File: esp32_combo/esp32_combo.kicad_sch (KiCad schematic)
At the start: 34 parts, among them J1 TERM BLK 3.5MM 2P SIDE, J2 TERM BLK 3.5MM 6P SIDE, J3 TERM BLK 3.5MM 6P SIDE, J4 TERM BLK 3.5MM 3P SIDE, J5 TERM BLK 3.5MM 3P SIDE, J6 HDR SKT 5PIN VERT 2.54MM, J7 HDR SKT 7PIN VERT 2.54MM, J8 SKT 2x6PIN VERT 2.54MM, J9 HDR SKT 8PIN VERT 2.54MM, Q1 AS2302, SW1 SS12D10, U1 TB6612FNG Module, U2 ESP32 DEV KIT Module 30-pin, U3 LM2596 Module

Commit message: Logo
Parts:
- removed J7: HDR SKT 7PIN VERT 2.54MM, Connector_PinSocket_2.54mm:PinSocket_1x07_P2.54mm_Vertical, symbol Makerspet:Conn_01x07_Key2
- added J7: HDR SKT 6PIN VERT 2.54MM, Connector_PinSocket_2.54mm:PinSocket_1x06_P2.54mm_Vertical, symbol Connector_Generic:Conn_01x06
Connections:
- net +5V: now also J7.2 (Pin_2)
- net GND: now also J7.1 (Pin_1)
- net GPIO18: now also J7.4 (Pin_4)
- net GPIO27: now also J7.3 (Pin_3)
- net GPIO4: now also J7.6 (Pin_6)
- net GPIO5_BOOT_STRAP: now also J7.5 (Pin_5)
- net LDS_EN: now also J9.6 (Pin_6); no longer J9.8 (Pin_8)
- net LDS_PWM: now also J9.5 (Pin_5); no longer J9.6 (Pin_6)
- net LDS_RX: now also J9.8 (Pin_8); no longer J9.7 (Pin_7)
- net MOT: now reaches D1.2 (A), J9.4 (Pin_4), Q1.3 (D)
- net at R11.2: now also J9.7 (Pin_7); no longer J9.5 (Pin_5)
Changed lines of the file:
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@@
   (junction (at 194.31 78.74) (diameter 0) (color 0 0 0 0)
   )
+  (junction (at 242.57 120.65) (diameter 0) (color 0 0 0 0)
+  )
   (junction (at 149.86 153.67) (diameter 0) (color 0 0 0 0)
   )
@@
   )
   (junction (at 55.88 115.57) (diameter 0) (color 0 0 0 0)
-  )
-  (junction (at 243.84 29.21) (diameter 0) (color 0 0 0 0)
-  )
-  (junction (at 242.57 123.19) (diameter 0) (color 0 0 0 0)
   )
   (no_connect (at 34.29 24.13))
@@
     (stroke (width 0) (type default))
   )
-  (wire (pts (xy 243.84 26.67) (xy 243.84 29.21))
-    (stroke (width 0) (type default))
-  )
   (wire (pts (xy 86.36 115.57) (xy 86.36 116.84))
     (stroke (width 0) (type default))
@@
     (stroke (width 0) (type default))
   )
-  (wire (pts (xy 229.87 123.19) (xy 242.57 123.19))
+  (wire (pts (xy 229.87 123.19) (xy 250.19 123.19))
     (stroke (width 0) (type default))
   )
@@
     (stroke (width 0) (type default))
   )
-  (wire (pts (xy 242.57 123.19) (xy 242.57 151.13))
-    (stroke (width 0) (type default))
-  )
   (wire (pts (xy 86.36 105.41) (xy 86.36 97.79))
     (stroke (width 0) (type default))
@@
     (stroke (width 0) (type default))
   )
-  (wire (pts (xy 229.87 125.73) (xy 250.19 125.73))
-    (stroke (width 0) (type default))
-  )
   (wire (pts (xy 149.86 152.4) (xy 149.86 153.67))
     (stroke (width 0) (type default))
@@
     (stroke (width 0) (type default))
   )
+  (wire (pts (xy 229.87 120.65) (xy 242.57 120.65))
+    (stroke (width 0) (type default))
+  )
   (wire (pts (xy 189.23 35.56) (xy 189.23 44.45))
     (stroke (width 0) (type default))
@@
     (stroke (width 0) (type default))
   )
-  (wire (pts (xy 229.87 120.65) (xy 236.22 120.65))
-    (stroke (width 0) (type default))
-  )
   (wire (pts (xy 43.18 113.03) (xy 57.15 113.03))
     (stroke (width 0) (type default))
@@
     (stroke (width 0) (type default))
   )
-  (wire (pts (xy 245.11 26.67) (xy 243.84 26.67))
-    (stroke (width 0) (type default))
-  )
   (wire (pts (xy 34.29 57.15) (xy 30.48 57.15))
     (stroke (width 0) (type default))
@@
     (stroke (width 0) (type default))
   )
+  (wire (pts (xy 236.22 125.73) (xy 229.87 125.73))
+    (stroke (width 0) (type default))
+  )
   (wire (pts (xy 55.88 115.57) (xy 55.88 116.84))
     (stroke (width 0) (type default))
@@
     (stroke (width 0) (type default))
   )
-  (wire (pts (xy 236.22 120.65) (xy 236.22 118.11))
+  (wire (pts (xy 236.22 118.11) (xy 236.22 125.73))
     (stroke (width 0) (type default))
   )
@@
     (stroke (width 0) (type default))
   )
+  (wire (pts (xy 242.57 120.65) (xy 250.19 120.65))
+    (stroke (width 0) (type default))
+  )
   (wire (pts (xy 143.51 36.83) (xy 162.56 36.83))
     (stroke (width 0) (type default))
@@
     (stroke (width 0) (type default))
   )
+  (wire (pts (xy 242.57 120.65) (xy 242.57 151.13))
+    (stroke (width 0) (type default))
+  )
   (wire (pts (xy 13.97 54.61) (xy 34.29 54.61))
     (stroke (width 0) (type default))
@@
   )
   (wire (pts (xy 143.51 57.15) (xy 144.78 57.15))
-    (stroke (width 0) (type default))
-  )
-  (wire (pts (xy 242.57 123.19) (xy 250.19 123.19))
     (stroke (width 0) (type default))
   )
@@
     (effects (font (size 1.27 1.27)) (justify left bottom))
   )
+  (label "LDS_TX" (at 250.19 118.11 180) (fields_autoplaced)
+    (effects (font (size 1.27 1.27)) (justify right bottom))
+  )
   (label "ENC_A_LEFT" (at 13.97 31.75 0) (fields_autoplaced)
     (effects (font (size 1.27 1.27)) (justify left bottom))
@@
     (effects (font (size 1.27 1.27)) (justify right bottom))
   )
+  (label "MOT" (at 234.95 118.11 180) (fields_autoplaced)
+    (effects (font (size 1.27 1.27)) (justify right bottom))
+  )
   (label "CW_LEFT" (at 162.56 24.13 180) (fields_autoplaced)
     (effects (font (size 1.27 1.27)) (justify right bottom))
   )
-  (label "LDS_TX" (at 250.19 118.11 180) (fields_autoplaced)
-    (effects (font (size 1.27 1.27)) (justify right bottom))
-  )
   (label "M+LEFT" (at 49.53 132.08 0) (fields_autoplaced)
     (effects (font (size 1.27 1.27)) (justify left bottom))
@@
     (effects (font (size 1.27 1.27)) (justify right bottom))
   )
+  (label "LDS_RX" (at 250.19 128.27 180) (fields_autoplaced)
+    (effects (font (size 1.27 1.27)) (justify right bottom))
+  )
   (label "ENC_B_RIGHT" (at 125.73 139.7 180) (fields_autoplaced)
     (effects (font (size 1.27 1.27)) (justify right bottom))
@@
     (effects (font (size 1.27 1.27)) (justify left bottom))
   )
-  (label "LDS_PWM" (at 250.19 123.19 180) (fields_autoplaced)
-    (effects (font (size 1.27 1.27)) (justify right bottom))
-  )
   (label "CW_LEFT" (at 109.22 110.49 180) (fields_autoplaced)
     (effects (font (size 1.27 1.27)) (justify right bottom))
@@
     (effects (font (size 1.27 1.27)) (justify left bottom))
   )
-  (label "LDS_RX" (at 250.19 125.73 180) (fields_autoplaced)
-    (effects (font (size 1.27 1.27)) (justify right bottom))
-  )
   (label "I2C_SDA" (at 179.07 78.74 0) (fields_autoplaced)
     (effects (font (size 1.27 1.27)) (justify left bottom))
@@
     (effects (font (size 1.27 1.27)) (justify left bottom))
   )
+  (label "LDS_PWM" (at 250.19 120.65 180) (fields_autoplaced)
+    (effects (font (size 1.27 1.27)) (justify right bottom))
+  )
   (label "I2C_INT" (at 179.07 81.28 0) (fields_autoplaced)
     (effects (font (size 1.27 1.27)) (justify left bottom))
@@
     (effects (font (size 1.27 1.27)) (justify right bottom))
   )
+  (label "LDS_EN" (at 250.19 123.19 180) (fields_autoplaced)
+    (effects (font (size 1.27 1.27)) (justify right bottom))
+  )
   (label "PWM_LEFT" (at 109.22 107.95 180) (fields_autoplaced)
     (effects (font (size 1.27 1.27)) (justify right bottom))
@@
   )
   (label "GPIO4" (at 162.56 49.53 180) (fields_autoplaced)
-    (effects (font (size 1.27 1.27)) (justify right bottom))
-  )
-  (label "LDS_EN" (at 250.19 128.27 180) (fields_autoplaced)
     (effects (font (size 1.27 1.27)) (justify right bottom))
   )
@@
         (path "/e24ae185-8f18-408c-aee8-f727519bade3"
           (reference "#PWR08") (unit 1)
-        )
-      )
-    )
-  )
-  (symbol (lib_id "Makerspet:Conn_01x07_Key2") (at 250.19 34.29 0) (unit 1)
-    (in_bom yes) (on_board yes) (dnp no)
-    (property "Reference" "J7" (at 249.174 23.622 0)
-      (effects (font (size 1.27 1.27)) (justify left))
-    )
-    (property "Value" "HDR SKT 7PIN VERT 2.54MM" (at 254 47.498 90)
-      (effects (font (size 1.27 1.27)) (justify left))
-    )
-    (property "Footprint" "Connector_PinSocket_2.54mm:PinSocket_1x07_P2.54mm_Vertical" (at 250.19 34.29 0)
-      (effects (font (size 1.27 1.27)) hide)
-    )
-    (property "Datasheet" "~" (at 250.19 34.29 0)
-      (effects (font (size 1.27 1.27)) hide)
-    )
-    (pin "5")
-    (pin "3")
-    (pin "2")
-    (pin "6")
-    (pin "1")
-    (pin "4")
-    (pin "7")
-    (instances
-      (project "esp32_combo"
-        (path "/e24ae185-8f18-408c-aee8-f727519bade3"
-          (reference "J7") (unit 1)
         )
       )
@@
         )
       )
+    )
+  )
+  (symbol (lib_id "Connector_Generic:Conn_01x06") (at 250.19 34.29 0) (unit 1)
+    (in_bom yes) (on_board yes) (dnp no)
+    (property "Reference" "J7" (at 248.92 25.4 0)
+      (effects (font (size 1.27 1.27)) (justify left))
+    )
+    (property "Value" "HDR SKT 6PIN VERT 2.54MM" (at 254 46.99 90)
+      (effects (font (size 1.27 1.27)) (justify left))
+    )
+    (property "Footprint" "Connector_PinSocket_2.54mm:PinSocket_1x06_P2.54mm_Vertical" (at 250.19 34.29 0)
+      (effects (font (size 1.27 1.27)) hide)
+    )
+    (property "Datasheet" "~" (at 250.19 34.29 0)
+      (effects (font (size 1.27 1.27)) hide)
+    )
+    (pin "6")
+    (pin "3")
+    (pin "4")
+    (pin "1")
+    (pin "5")
+    (pin "2")
+    (instances
+      (project "esp32_combo"
+        (path "/e24ae185-8f18-408c-aee8-f727519bade3"
+          (reference "J7") (unit 1)
+        )
+      )

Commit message: Combo tweaks
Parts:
- removed C2: 100uF 16V, Capacitor_Tantalum_SMD:CP_EIA-7343-15_Kemet-W, symbol Device:C_Polarized_Small_US
- C1: value 22uF -> 22uF 6.3V
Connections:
- net EA_LEFT renamed EA_LEFT_FG
- net EA_RIGHT renamed EA_RIGHT_FG
- net ENC_A_LEFT renamed ENC_A_LEFT_FG
- net ENC_A_RIGHT renamed ENC_A_RIGHT_FG
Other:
- note added: "INPUT VOLTAGE 9..13.5V WHEN USING TB6612FNG - Use 12V brushed motors Max input current approx. 3.0A with both motors stalled Safety - motor power overcurrent protection using a fuse Use a slow-blow fuse to prevent inrush current tripping the fuse - battery input reverse polarity protection using a Schottki diode - TODO input overvoltage LM2596 40V max; motors not protected - TODO 5V output LM2596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"
- note removed: "Input voltage 9..13.5V - Use 12V motors Max input current approx. 3.0A with both motors stalled Safety - motor power overcurrent protection using a fuse Use a slow-blow fuse to prevent inrush current tripping the fuse - battery input reverse polarity protection using a Schottki diode - TODO input overvoltage LM2596 40V max; motors not protected - TODO 5V output LM2596 provides current limit, shor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"
- moved on the sheet: C1

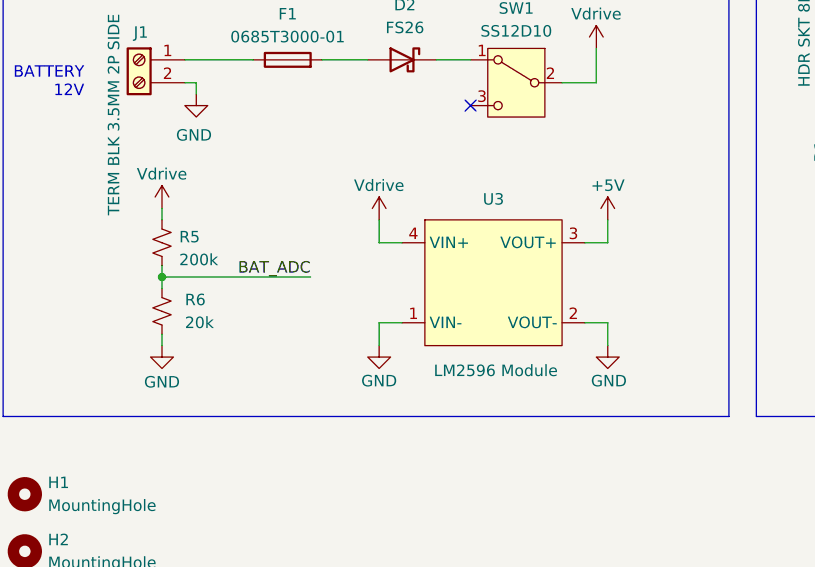
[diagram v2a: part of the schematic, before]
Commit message: 1% resistor divider
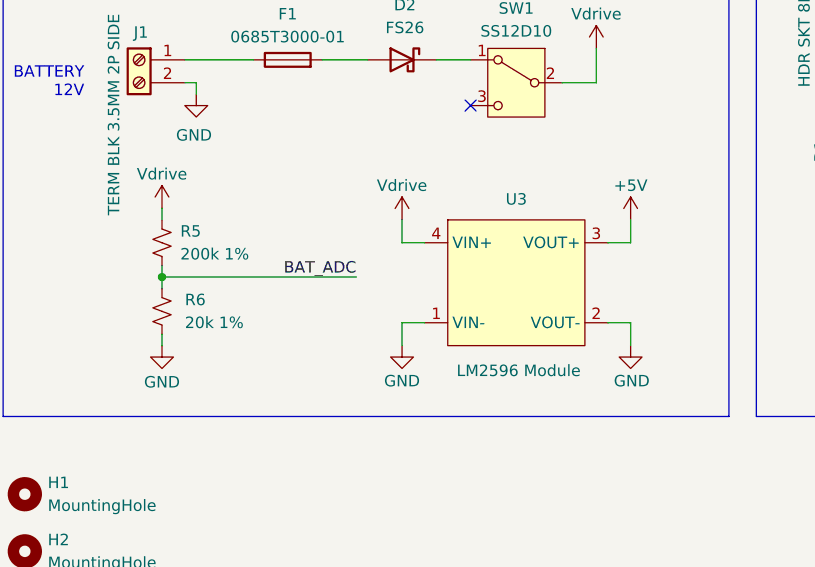
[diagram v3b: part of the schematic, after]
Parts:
- R5: value 200k -> 200k 1%
- R6: value 20k -> 20k 1%
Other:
- moved on the sheet: U3
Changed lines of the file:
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@@
 	(wire
 		(pts
-			(xy 173.99 149.86) (xy 176.53 149.86)
+			(xy 176.53 149.86) (xy 179.07 149.86)
 		)
 		(stroke
@@
 	(wire
 		(pts
-			(xy 173.99 158.75) (xy 176.53 158.75)
+			(xy 176.53 158.75) (xy 179.07 158.75)
 		)
 		(stroke
@@
 	(wire
 		(pts
-			(xy 173.99 161.29) (xy 173.99 158.75)
+			(xy 176.53 161.29) (xy 176.53 158.75)
 		)
 		(stroke
@@
 	(wire
 		(pts
-			(xy 199.39 161.29) (xy 199.39 158.75)
+			(xy 201.93 161.29) (xy 201.93 158.75)
 		)
 		(stroke
@@
 	(wire
 		(pts
-			(xy 196.85 149.86) (xy 199.39 149.86)
+			(xy 199.39 149.86) (xy 201.93 149.86)
 		)
 		(stroke
@@
 	(wire
 		(pts
-			(xy 196.85 158.75) (xy 199.39 158.75)
+			(xy 199.39 158.75) (xy 201.93 158.75)
 		)
 		(stroke
@@
 	(wire
 		(pts
-			(xy 173.99 147.32) (xy 173.99 149.86)
+			(xy 176.53 147.32) (xy 176.53 149.86)
 		)
 		(stroke
@@
 	(wire
 		(pts
-			(xy 149.86 153.67) (xy 166.37 153.67)
+			(xy 149.86 153.67) (xy 171.45 153.67)
 		)
 		(stroke
@@
 	(wire
 		(pts
-			(xy 199.39 147.32) (xy 199.39 149.86)
+			(xy 201.93 147.32) (xy 201.93 149.86)
 		)
 		(stroke
@@
 		)
 	)
+	(label "BAT_ADC"
+		(at 171.45 153.67 180)
+		(fields_autoplaced yes)
+		(effects
+			(font
+				(size 1.27 1.27)
+			)
+			(justify right bottom)
+		)
+	)
 	(label "M+LEFT"
 		(at 43.18 110.49 0)
@@
 		)
 	)
-	(label "BAT_ADC"
-		(at 166.37 153.67 180)
-		(fields_autoplaced yes)
-		(effects
-			(font
-				(size 1.27 1.27)
-			)
-			(justify right bottom)
-		)
-	)
 	(label "LDS_RX"
 		(at 250.19 128.27 180)
@@
 	(symbol
 		(lib_id "power:GND")
-		(at 173.99 161.29 0)
+		(at 176.53 161.29 0)
 		(unit 1)
 		(exclude_from_sim no)
@@
 		(dnp no)
 		(property "Reference" "#PWR022"
-			(at 173.99 167.64 0)
+			(at 176.53 167.64 0)
 			(effects
 				(font
@@
 		)
 		(property "Value" "GND"
-			(at 173.99 165.227 0)
+			(at 176.53 165.227 0)
 			(effects
 				(font
@@
 		)
 		(property "Footprint" ""
-			(at 173.99 161.29 0)
+			(at 176.53 161.29 0)
 			(effects
 				(font
@@
 		)
 		(property "Datasheet" ""
-			(at 173.99 161.29 0)
+			(at 176.53 161.29 0)
 			(effects
 				(font
@@
 		)
 		(property "Description" "Power symbol creates a global label with name \"GND\" , ground"
-			(at 173.99 161.29 0)
+			(at 176.53 161.29 0)
 			(effects
 				(font
@@
 	(symbol
 		(lib_id "Makerspet:LM2596 Module")
-		(at 186.69 144.78 0)
+		(at 189.23 144.78 0)
 		(unit 1)
 		(exclude_from_sim no)
@@
 		(dnp no)
 		(property "Reference" "U3"
-			(at 186.69 145.034 0)
+			(at 189.23 145.034 0)
 			(effects
 				(font
@@
 		)
 		(property "Value" "LM2596 Module"
-			(at 186.944 164.084 0)
+			(at 189.484 164.084 0)
 			(effects
 				(font
@@
 		)
 		(property "Footprint" "Makerspet:LM2596 Module SMD"
-			(at 186.69 143.51 0)
+			(at 189.23 143.51 0)
 			(effects
 				(font
@@
 		)
 		(property "Datasheet" ""
-			(at 186.69 144.78 0)
+			(at 189.23 144.78 0)
 			(effects
 				(font
@@
 		)
 		(property "Description" ""
-			(at 186.69 144.78 0)
+			(at 189.23 144.78 0)
 			(effects
 				(font
@@
 		)
 		(property "Type" ""
-			(at 186.69 142.24 0)
+			(at 189.23 142.24 0)
 			(effects
 				(font
@@
 		)
 		(property "Link" "https://www.amazon.com/Zixtec-LM2596-Converter-Module-1-25V-30V/dp/B07VVXF7YX/"
-			(at 187.96 140.335 0)
+			(at 190.5 140.335 0)
 			(effects
 				(font
@@
 		(fields_autoplaced yes)
 		(property "Reference" "R6"
-			(at 152.4 156.21 0)
+			(at 152.4 156.2099 0)
 			(effects
 				(font
@@
 			)
 		)
-		(property "Value" "20k"
-			(at 152.4 158.75 0)
+		(property "Value" "20k 1%"
+			(at 152.4 158.7499 0)
 			(effects
 				(font
@@
 	(symbol
 		(lib_id "power:Vdrive")
-		(at 173.99 147.32 0)
+		(at 176.53 147.32 0)
 		(unit 1)
 		(exclude_from_sim no)
@@
 		(dnp no)
 		(property "Reference" "#PWR021"
-			(at 168.91 151.13 0)
+			(at 171.45 151.13 0)
 			(effects
 				(font
@@
 		)
 		(property "Value" "Vdrive"
-			(at 173.99 143.51 0)
+			(at 176.53 143.51 0)
 			(effects
 				(font
@@
 		)
 		(property "Footprint" ""
-			(at 173.99 147.32 0)
+			(at 176.53 147.32 0)
 			(effects
 				(font
@@
 		)
 		(property "Datasheet" ""
-			(at 173.99 147.32 0)
+			(at 176.53 147.32 0)
 			(effects
 				(font
@@
 		)
 		(property "Description" "Power symbol creates a global label with name \"Vdrive\""
-			(at 173.99 147.32 0)
+			(at 176.53 147.32 0)
 			(effects
 				(font
@@
 		(on_board yes)
 		(dnp no)
-		(fields_autoplaced yes)
 		(property "Reference" "R5"
-			(at 151.765 149.225 0)
+			(at 151.892 148.59 0)
 			(effects
 				(font
@@
 			)
 		)
-		(property "Value" "200k"
-			(at 151.765 151.765 0)
+		(property "Value" "200k 1%"
+			(at 151.892 151.13 0)
 			(effects
 				(font
@@
 	(symbol
 		(lib_id "power:GND")
-		(at 199.39 161.29 0)
+		(at 201.93 161.29 0)
 		(unit 1)
 		(exclude_from_sim no)
@@
 		(dnp no)
 		(property "Reference" "#PWR028"
-			(at 199.39 167.64 0)
+			(at 201.93 167.64 0)
 			(effects
 				(font
@@
 		)
 		(property "Value" "GND"
-			(at 199.517 165.227 0)
+			(at 202.057 165.227 0)
 			(effects
 				(font
@@
 		)
 		(property "Footprint" ""
-			(at 199.39 161.29 0)
+			(at 201.93 161.29 0)
 			(effects
 				(font
@@
 		)
 		(property "Datasheet" ""
-			(at 199.39 161.29 0)
+			(at 201.93 161.29 0)
 			(effects
 				(font
@@
 		)
 		(property "Description" "Power symbol creates a global label with name \"GND\" , ground"
-			(at 199.39 161.29 0)
+			(at 201.93 161.29 0)
 			(effects
 				(font
@@
 	(symbol
 		(lib_id "power:+5V")
-		(at 199.39 147.32 0)
+		(at 201.93 147.32 0)
 		(unit 1)
 		(exclude_from_sim no)
@@
 		(fields_autoplaced yes)
 		(property "Reference" "#PWR027"
-			(at 199.39 151.13 0)
+			(at 201.93 151.13 0)
 			(effects
 				(font
@@
 		)
 		(property "Value" "+5V"
-			(at 199.39 143.51 0)
+			(at 201.93 143.51 0)
 			(effects
 				(font
@@
 		)
 		(property "Footprint" ""
-			(at 199.39 147.32 0)
+			(at 201.93 147.32 0)
 			(effects
 				(font
@@
 		)
 		(property "Datasheet" ""
-			(at 199.39 147.32 0)
+			(at 201.93 147.32 0)
 			(effects
 				(font
@@
 		)
 		(property "Description" "Power symbol creates a global label with name \"+5V\""
-			(at 199.39 147.32 0)
+			(at 201.93 147.32 0)
 			(effects
 				(font

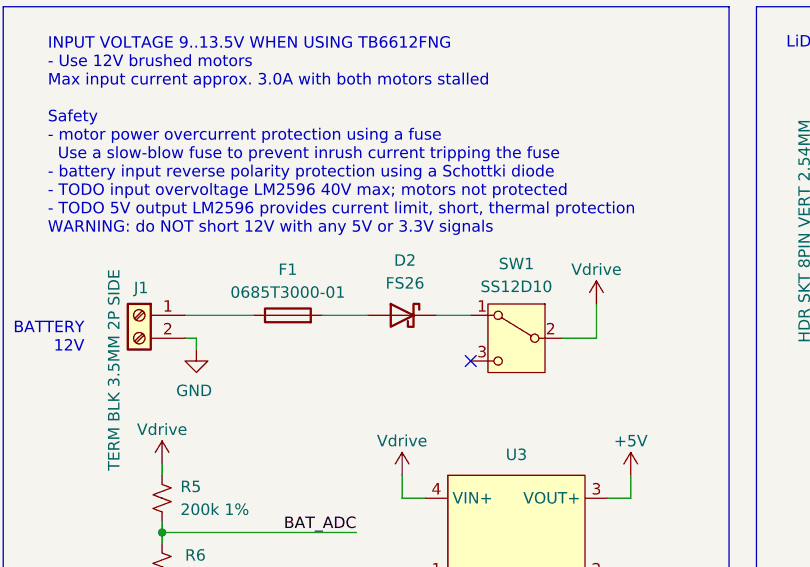
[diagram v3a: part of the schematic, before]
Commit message: 3A diode
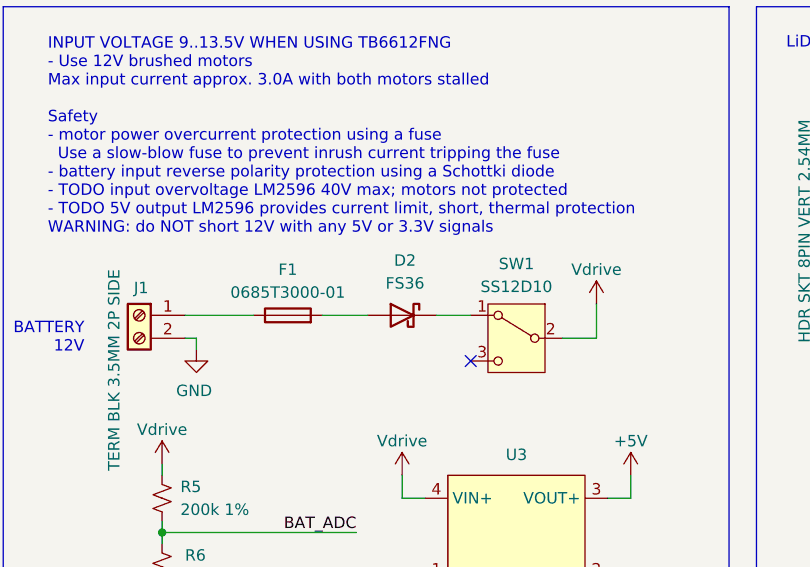
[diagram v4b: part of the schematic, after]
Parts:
- D2: value FS26 -> FS36
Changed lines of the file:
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@@
 			)
 		)
-		(property "Value" "FS26"
+		(property "Value" "FS36"
 			(at 176.8475 125.984 0)
 			(effects
@@
 			)
 		)
-		(property "Datasheet" "https://www.digikey.com/en/products/detail/good-ark-semiconductor/FS26/18667798"
+		(property "Datasheet" "https://www.digikey.com/en/products/detail/good-ark-semiconductor/FS36/18648966"
 			(at 176.53 129.54 0)
 			(effects
